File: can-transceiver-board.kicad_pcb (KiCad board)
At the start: 2 copper layers, 20 x 13 mm, 5 parts, among them K1 JMP, P1 CONN_5, U1 MAX3051

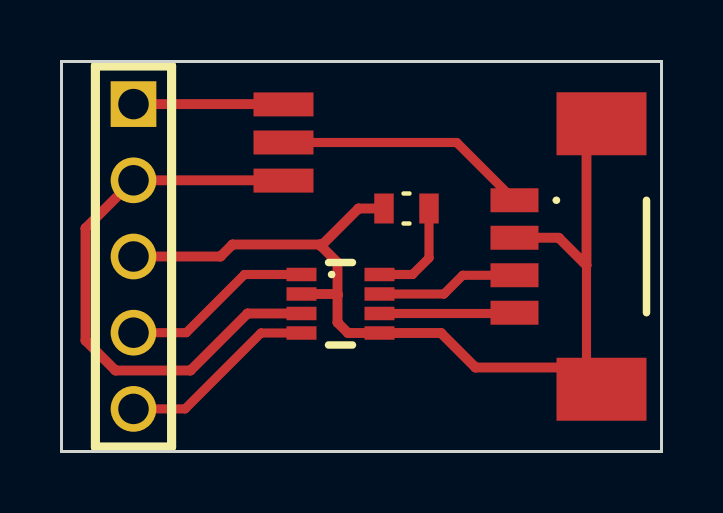
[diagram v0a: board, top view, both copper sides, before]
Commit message: Improved GND routing, added CAN terminal resistor pin.
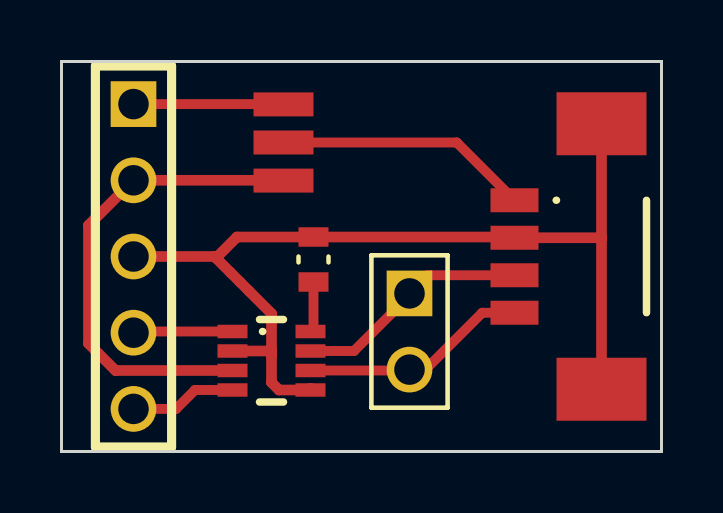
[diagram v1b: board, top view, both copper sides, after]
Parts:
- added R2: opt, PIN_ARRAY_2X1, F.Cu at (31.6, 29.0)
- moved R1 3.54 mm to (28.4, 26.6), turned to 90 degrees
- moved U1 2.98 mm to (25.7, 29.0)
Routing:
- net /3V3: track 19.4 -> 16.2 mm
- net Net-(CONN1-Pad3): track 4.76 -> 7.89 mm
- net Net-(CONN1-Pad4): track 4.51 -> 7.63 mm
- net /RXD: track 6.65 -> 3.56 mm
- net /TXD: track 6.40 -> 3.32 mm
- net GND: track 34.9 -> 32.6 mm
- net Net-(R1-Pad1): track 3.53 -> 1.69 mm
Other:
- net class Default: trace_width 0.3048 -> 0.3302
- net class fat: clearance 0.254 -> 0.2286; trace_width 0.3302 -> 0.3556
